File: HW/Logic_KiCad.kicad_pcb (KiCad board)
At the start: 4 copper layers, 100 x 100 mm, 267 parts, among them J1 USB_B_Micro, J2 USB_C_Receptacle_USB2.0, Q1 Q_NPN_BEC, Q10 Q_NMOS_GSD, Q11 Q_NMOS_GSD, Q2 Q_NPN_BEC, Q3 Q_NMOS_GSD, Q4 Q_NMOS_GSD, Q5 Q_PMOS_GSD, Q6 Q_NMOS_GSD, Q7 Q_PMOS_GSD, Q8 Q_NMOS_GSD, Q9 Q_PMOS_GSD, SW1 SW_SPDT, SW10 button, SW11 button, SW12 button, SW13 SW_SPST, SW14 SW_SPST, SW15 SW_SPST, SW2 button, SW3 button, SW4 button, SW5 button, SW6 button, SW7 button, SW8 button, SW9 button, U1 ESP32-PICO-D4, U2 CP2102N-A01-GQFN28, U3 SY8105

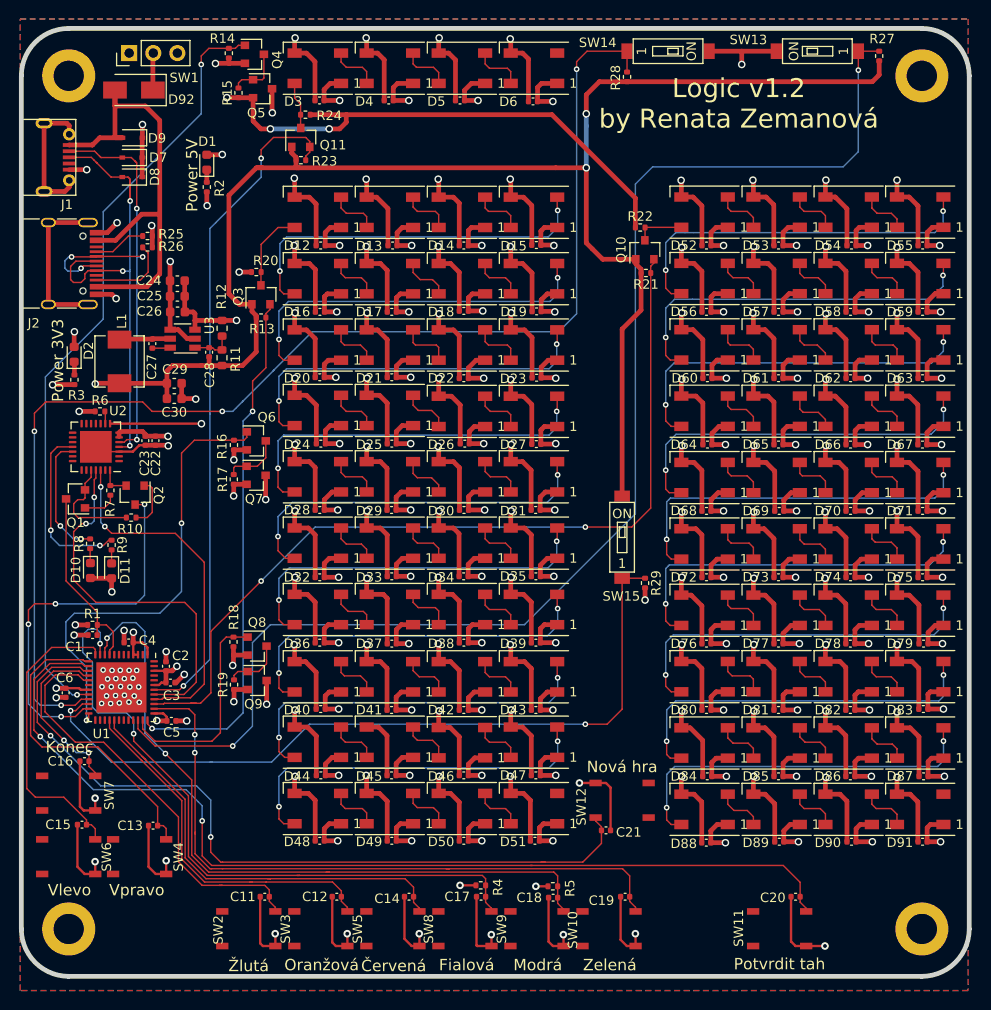
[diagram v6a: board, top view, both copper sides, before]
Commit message: add tooling holes
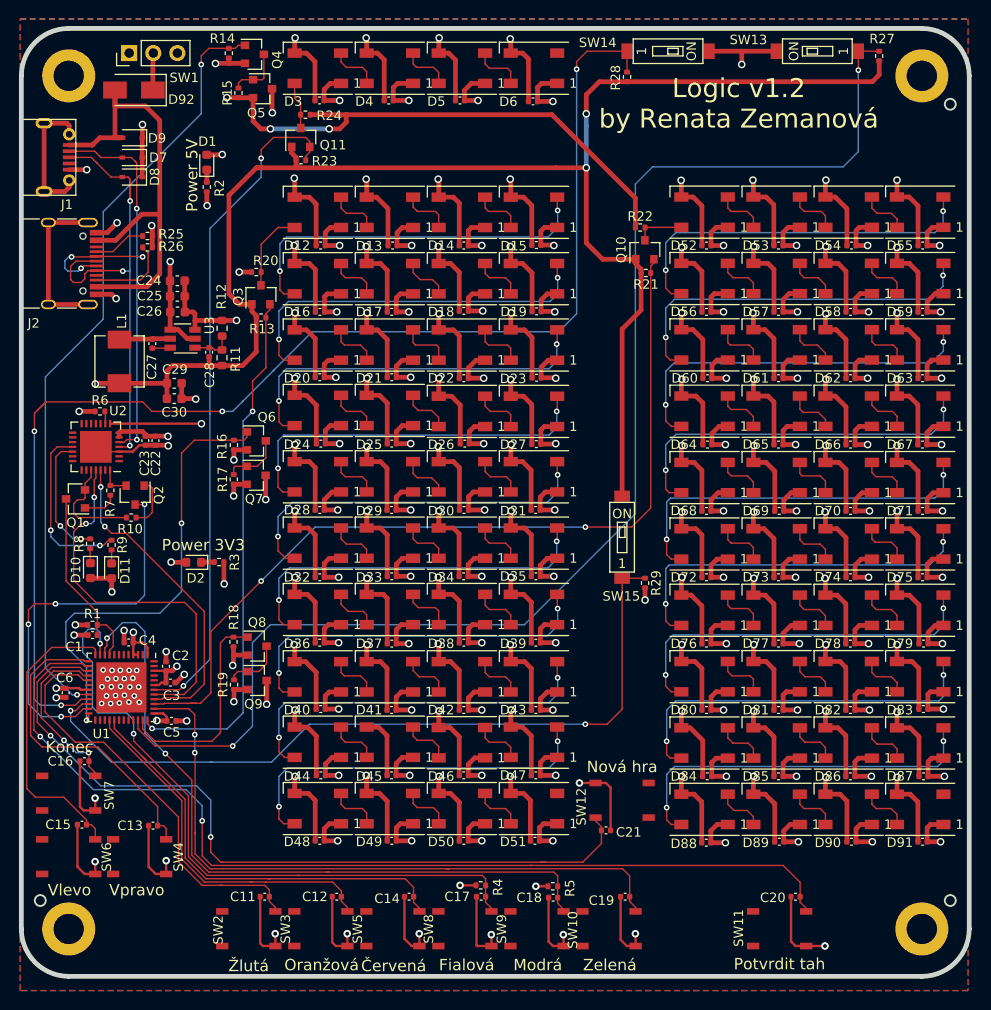
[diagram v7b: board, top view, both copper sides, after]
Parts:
- moved D2 25.3 mm to (113.2, 91.3), turned to 180 degrees
- moved R3 24.6 mm to (115.9, 91.3), turned to 180 degrees
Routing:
- net RX_ESP: track 37.0 -> 34.0 mm
- net PREPINAC_1: track 133.8 -> 135.0 mm
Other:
- outline, holes or cut-outs redrawn
